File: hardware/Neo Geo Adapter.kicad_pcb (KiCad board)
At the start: 4 copper layers, 60 x 60 mm, 25 parts, among them J101 AVR-UPDI-6, J102 Playstation, J103 Saturn, J104 NEO_GEO, SW101 AF_A, SW102 AF_B, SW103 AF_C, SW104 AF_D, SW105 AUTO, SW106 MODE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

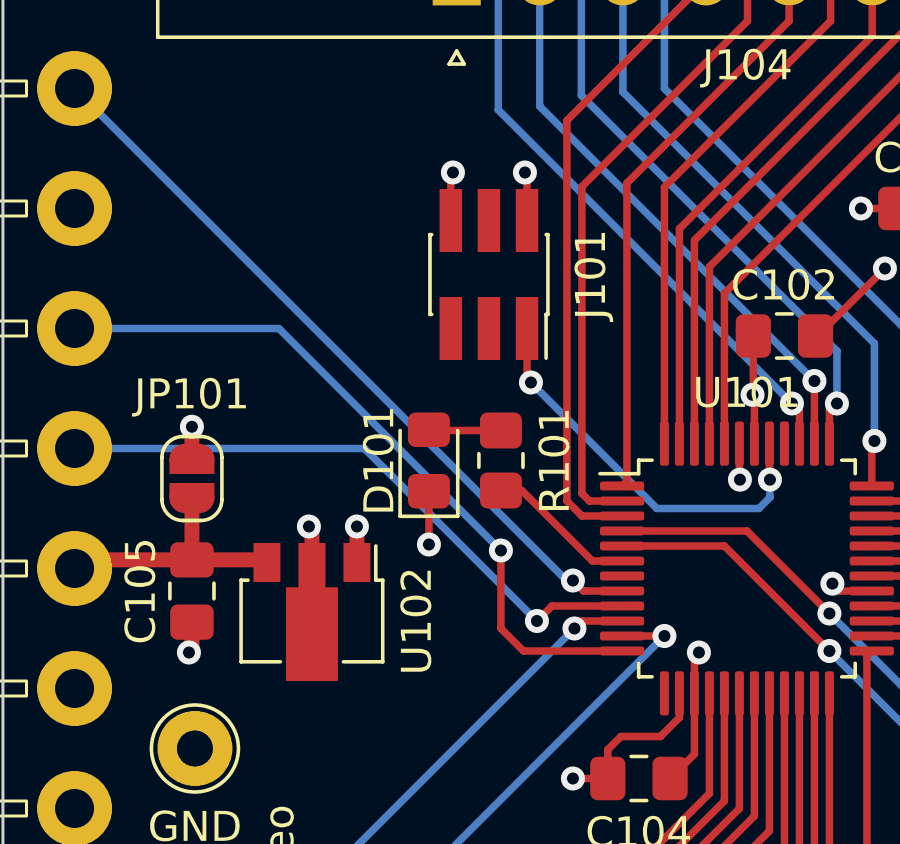
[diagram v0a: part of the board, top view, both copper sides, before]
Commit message: Fixed PDI header gender, KiCad 8
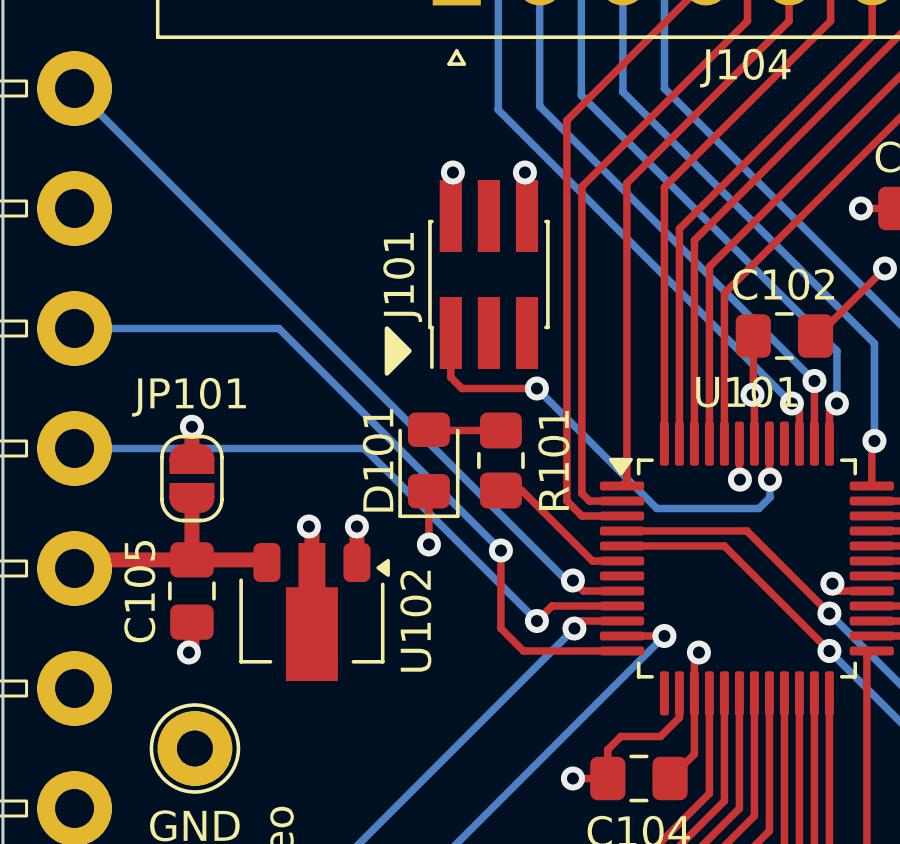
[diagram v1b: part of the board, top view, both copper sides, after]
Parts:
- J101: footprint Connector_PinSocket_1.27mm:PinSocket_2x03_P1.27mm_Vertical_SMD -> Connector_PinHeader_1.27mm:PinHeader_2x03_P1.27mm_Vertical_SMD
- turned J101 to 90 degrees
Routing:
- net /UPDI_DATA: track 13.5 -> 15.9 mm

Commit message: Added top board with labelling
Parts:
- moved J103 4.70 mm to (103.0, 96.0)
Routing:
- net /MODE1: track 64.7 -> 32.5 mm, vias 0 -> 1
- net /MODE2: track 69.5 -> 42.2 mm, vias 0 -> 1
- net /SAT_D2: track 18.6 -> 15.1 mm
- net /SAT_D3: track 16.6 -> 13.1 mm
- net /SAT_TR: track 16.0 -> 12.6 mm
- net /SAT_TL: track 15.4 -> 12.0 mm
- net /SAT_TH: track 16.6 -> 14.2 mm
- net /SAT_D0: track 17.3 -> 15.9 mm
- net /AUTO2: track 68.4 -> 67.7 mm
- net /AUTO1: track 63.9 -> 64.6 mm
- net /SAT_D1: track 17.9 -> 17.2 mm
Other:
- outline, holes or cut-outs redrawn
- board text added: "SAT/PS to Neo Geo"
- board text removed: "Saturn/Playstation to Neo Geo"

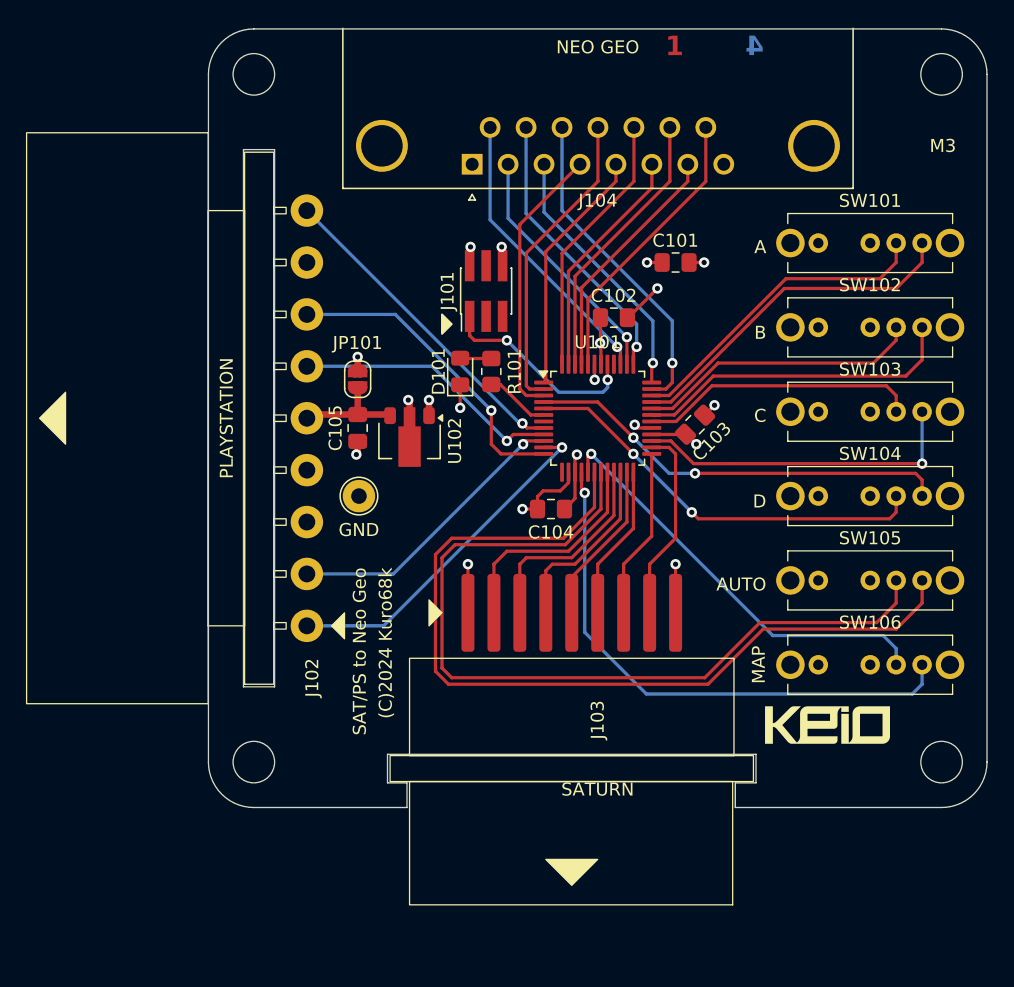
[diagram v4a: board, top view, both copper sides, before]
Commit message: Playstation 3V3 power and signalling
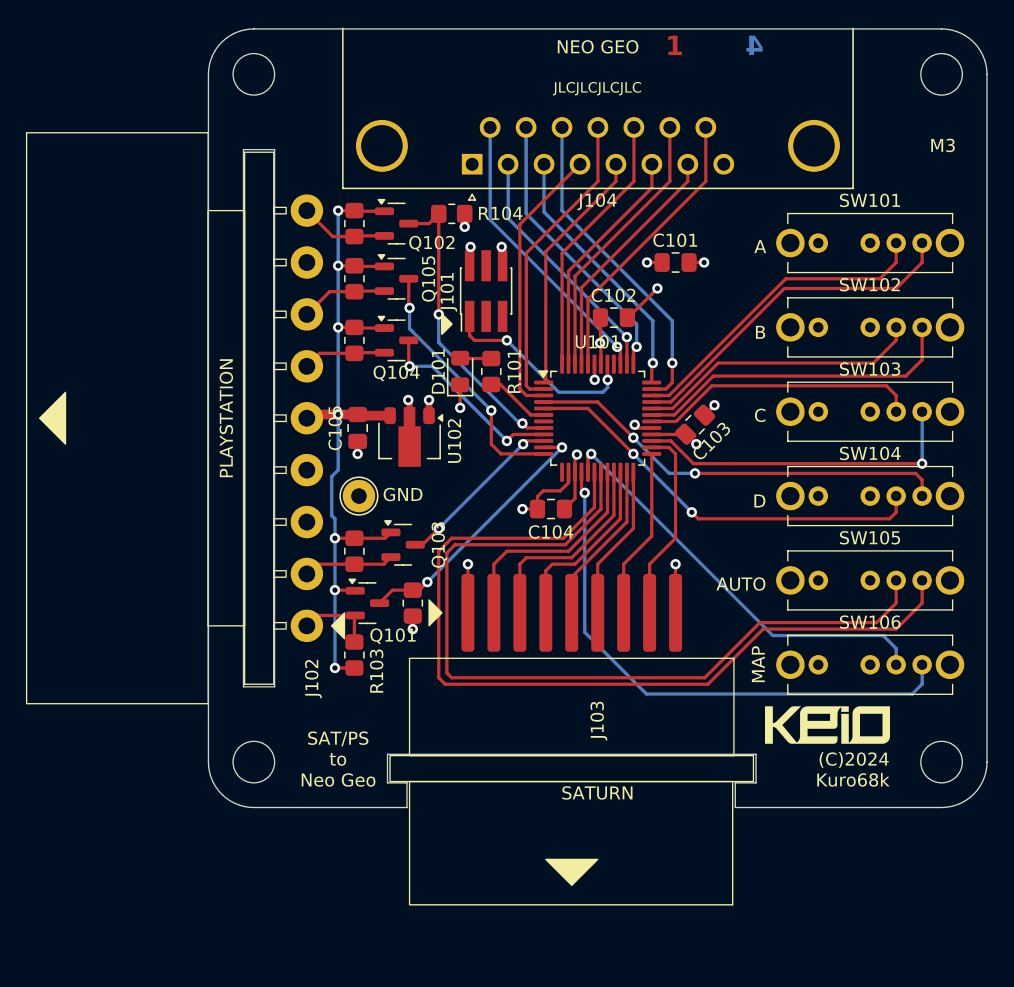
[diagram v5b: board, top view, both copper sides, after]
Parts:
- removed JP101: PS_5V, Jumper:SolderJumper-2_P1.3mm_Open_RoundedPad1.0x1.5mm
- added Q101: BSS138, Package_TO_SOT_SMD:SOT-23, F.Cu at (87.2, 84.2)
- added Q102: BSS138, Package_TO_SOT_SMD:SOT-23, F.Cu at (89.5, 55.0)
- added Q103: BSS138, Package_TO_SOT_SMD:SOT-23, F.Cu at (90.0, 79.8)
- added Q104: BSS138, Package_TO_SOT_SMD:SOT-23, F.Cu at (89.5, 64.0)
- added Q105: BSS138, Package_TO_SOT_SMD:SOT-23, F.Cu at (89.5, 59.2)
- added R102: 5k6, Resistor_SMD:R_0805_2012Metric_Pad1.20x1.40mm_HandSolder, F.Cu at (90.8, 84.2)
- added R103: 5k6, Resistor_SMD:R_0805_2012Metric_Pad1.20x1.40mm_HandSolder, F.Cu at (86.2, 88.2)
- added R104: 5k6, Resistor_SMD:R_0805_2012Metric_Pad1.20x1.40mm_HandSolder, F.Cu at (93.8, 54.2)
- added R105: 5k6, Resistor_SMD:R_0805_2012Metric_Pad1.20x1.40mm_HandSolder, F.Cu at (86.2, 55.0)
- added R107: 5k6, Resistor_SMD:R_0805_2012Metric_Pad1.20x1.40mm_HandSolder, F.Cu at (86.2, 80.2)
- added R109: 5k6, Resistor_SMD:R_0805_2012Metric_Pad1.20x1.40mm_HandSolder, F.Cu at (86.2, 64.0)
- added R111: 5k6, Resistor_SMD:R_0805_2012Metric_Pad1.20x1.40mm_HandSolder, F.Cu at (86.2, 59.2)
- R101: value 470Ω -> 5k6
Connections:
- J102 pad 1: /PS_DAT -> /PS_DAT_3V3
- J102 pad 2: /PS_CMD -> /PS_CMD_3V3
- J102 pad 6: /PS_ATT -> /PS_ATT_3V3
- J102 pad 7: /PS_CLK -> /PS_CLK_3V3
- J102 pad 9: /PS_ACK -> /PS_ACK_3V3
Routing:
- net +3.3V: track 8.63 -> 60.5 mm, vias 0 -> 7
- net /PS_CMD: track 22.5 -> 13.2 mm, vias 1 -> 2
- net /PS_CMD_3V3: track 0.00 -> 7.01 mm
- net /PS_ACK_3V3: track 0.00 -> 6.82 mm
- net /PS_CLK_3V3: track 0.00 -> 6.72 mm
- net /PS_ATT_3V3: track 0.00 -> 6.41 mm
- net /PS_DAT: track 26.8 -> 20.4 mm, vias 1 -> 2
- net /PS_DAT_3V3: track 0.00 -> 6.13 mm
- net /PS_ATT: track 20.8 -> 15.0 mm, vias 1 -> 2
- net /PS_CLK: track 24.2 -> 19.7 mm, vias 1 -> 2
- net /PS_ACK: track 25.2 -> 23.4 mm, vias 1 -> 2
- net +5V: track 22.1 -> 23.1 mm, vias 8 -> 9
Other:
- board text added: "JLCJLCJLCJLC"

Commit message: Rev 2 RTM
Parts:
- removed Q101, Q102: BSS138, Package_TO_SOT_SMD:SOT-23
- removed R102, R104: 5k6, Resistor_SMD:R_0805_2012Metric_Pad1.20x1.40mm_HandSolder
- U101: value AVR32DA48x-xPT -> AVR32EA48x-xPT
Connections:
- J102 pad 1: /PS_DAT_3V3 -> /PS_DAT
- J102 pad 9: /PS_ACK_3V3 -> /PS_ACK
- R103 pad 2: /PS_DAT_3V3 -> /PS_DAT
- R105 pad 2: /PS_ACK_3V3 -> /PS_ACK
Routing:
- net /PS_DAT: track 20.4 -> 28.8 mm
- net /PS_ACK_3V3: track 6.82 -> 0.00 mm
- net /PS_ACK: track 23.4 -> 29.7 mm
- net /PS_DAT_3V3: track 6.13 -> 0.00 mm
- net +3.3V: track 60.5 -> 56.6 mm, vias 7 -> 6
- net +5V: track 23.1 -> 21.1 mm, vias 9 -> 7
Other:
- board text added: "Rev2"
